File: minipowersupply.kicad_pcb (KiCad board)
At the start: 2 copper layers, 91 x 60.4 mm, 112 parts, among them J1 Conn_01x01_Female, J10 Conn_01x08_Male, J2 Conn_01x01_Female, J3 Conn_01x01_Female, J4 Conn_01x01_Female, J5 Conn_01x01_Female, J6 Conn_01x01_Female, J7 Conn_01x01_Female, J8 Conn_01x02_Female, J9 Conn_01x02_Female, Q1 BC817, U1 LM317_TO-220, U10 74HC4051, U11 74HC4051, U12 LM358, U13 LM358, U2 LM337_TO220, U3 LM7805_TO220, U4 ACS70331EOLCTR-2P5U3, U5 ACS70331EOLCTR-2P5U3, U6 ACS70331EOLCTR-2P5U3, U7 ACS70331EOLCTR-2P5U3, U8 ACS70331EOLCTR-2P5U3, U9 LM358

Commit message: new EMC-EMI layout with improved suppression
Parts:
- removed A1: Arduino_Nano_v3.x, Module:Arduino_Nano
- removed C1, C10, C11, C12, C13, C14, C15, C16, C17, C18, C19, C2, C22, C23, C24, C25, C27, C29, C3, C30, C31, C32, C33, C34, C35, C36, C38, C4, C5, C6, C7, C8, C9: 0.1uF, Capacitor_SMD:C_0603_1608Metric
- removed C20, C21: 150uF, Capacitor_SMD:C_Elec_8x6.2
- removed C26, C28: 1uF, Capacitor_SMD:C_0603_1608Metric
- removed D1, D2, D3, D4, D5, D6, D7, D8, D9: S1K-13-F, Diode_SMD:D_SMA
- removed F1: Fuse, Fuse:Fuseholder_Cylinder-5x20mm_Bulgin_FX0457_Horizontal_Closed
- removed J1, J2, J3, J4, J5, J6, J7: Conn_01x01_Female, Connector_PinHeader_2.54mm:PinHeader_1x01_P2.54mm_Vertical
- removed J10: Conn_01x08_Male, Connector_PinHeader_2.54mm:PinHeader_1x08_P2.54mm_Vertical
- removed J8, J9: Conn_01x02_Female, Connector_PinHeader_2.54mm:PinHeader_1x02_P2.54mm_Vertical
- removed Q1: BC817, Package_TO_SOT_SMD:SOT-23
- removed R1, R2: 240, Resistor_SMD:R_0603_1608Metric
- removed R10, R11, R12, R13, R14, R15, R16, R17, R18, R19, R20, R21, R22, R23, R24, R25, R26, R27, R28, R29, R30, R33, R34, R35, R36, R6, R7, R8, R9: 10k 0.01%, Resistor_SMD:R_0603_1608Metric
- removed R3: 4.420k, Resistor_SMD:R_0603_1608Metric
- removed R31, R32: 100k 0.01%, Resistor_SMD:R_0603_1608Metric
- removed R4: 698, Resistor_SMD:R_0603_1608Metric
- removed R5: 410, Resistor_SMD:R_0603_1608Metric
- removed TP1, TP2, TP3: TestPoint, TestPoint:TestPoint_THTPad_4.0x4.0mm_Drill2.0mm
- removed TR1: TRANSF3, minipowersupply:vtxtfr
- removed U1: LM317_TO-220, Package_TO_SOT_SMD:SOT-223-3_TabPin2
- removed U10, U11: 74HC4051, Package_SO:TSSOP-16_4.4x5mm_P0.65mm
- removed U12, U13, U9: LM358, Package_SO:TSSOP-8_4.4x3mm_P0.65mm
- removed U2: LM337_TO220, Package_TO_SOT_SMD:SOT-223-3_TabPin2
- removed U3: LM7805_TO220, Package_TO_SOT_SMD:SOT-223-3_TabPin2
- removed U4, U5, U6, U7, U8: ACS70331EOLCTR-2P5U3, ACS70331EOLCTR-2P5U3:SOIC127P600X175-8N
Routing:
- net GNDREF: track 289.1 -> 0.00 mm, vias 55 -> 0
- net VUnreg+: track 170.0 -> 0.00 mm, vias 6 -> 0
- net 3V3: track 164.9 -> 0.00 mm, vias 12 -> 0
- net VUnreg-: track 95.1 -> 0.00 mm, vias 8 -> 0
- net /Clock and TTL/Ck_Out: track 93.0 -> 0.00 mm, vias 1 -> 0
- net V5: track 90.4 -> 0.00 mm, vias 3 -> 0
- net /I V Sensor, Mux and output/A1: track 64.5 -> 0.00 mm, vias 4 -> 0
- net /I V Sensor, Mux and output/VU+: track 61.1 -> 0.00 mm, vias 2 -> 0
- net /I V Sensor, Mux and output/A3: track 60.8 -> 0.00 mm, vias 2 -> 0
- net /I V Sensor, Mux and output/A0: track 57.5 -> 0.00 mm, vias 2 -> 0
- net /I V Sensor, Mux and output/VA+: track 48.3 -> 0.00 mm, vias 1 -> 0
- net /I V Sensor, Mux and output/IU+: track 47.9 -> 0.00 mm, vias 2 -> 0
- net /I V Sensor, Mux and output/U- Unity Inverter/Ain: track 42.4 -> 0.00 mm, vias 2 -> 0
- net /I V Sensor, Mux and output/A2: track 42.2 -> 0.00 mm, vias 2 -> 0
- net /I V Sensor, Mux and output/A5: track 39.5 -> 0.00 mm
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- removed copper zone on B.Cu, net GNDREF
- removed copper zone on F.Cu, net GNDREF
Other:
- board outline removed
- board text removed: "5V"
- board text removed: "A+"
- board text removed: "A-"
- board text removed: "CK"
- board text removed: "Safety Cutouts"
- board text removed: "U+"
- board text removed: "U-"

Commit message: updates with foot print guard rings
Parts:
- added A1: Arduino_Nano_v3.x, Module:Arduino_Nano, F.Cu at (99.1, 125.7)
- added C1: 0.1uF, Capacitor_SMD:C_0603_1608Metric, B.Cu at (181.1, 66.5)
- added C10: 0.1uF, Capacitor_SMD:C_0603_1608Metric, F.Cu at (187.8, 96.4)
- added C11: 0.1uF, Capacitor_SMD:C_0603_1608Metric, F.Cu at (212.0, 73.6)
- added C12: 0.1uF, Capacitor_SMD:C_0603_1608Metric, F.Cu at (212.0, 77.0)
- added C13: 0.1uF, Capacitor_SMD:C_0603_1608Metric, F.Cu at (189.1, 106.5)
- added C14: 0.1uF, Capacitor_SMD:C_0603_1608Metric, F.Cu at (212.0, 83.7)
- added C15: 0.1uF, Capacitor_SMD:C_0603_1608Metric, F.Cu at (212.0, 86.8)
- added C16: 0.1uF, Capacitor_SMD:C_0603_1608Metric, F.Cu at (212.0, 89.3)
- added C17: 0.1uF, Capacitor_SMD:C_0603_1608Metric, F.Cu at (212.0, 92.5)
- added C18: 0.1uF, Capacitor_SMD:C_0603_1608Metric, F.Cu at (184.2, 112.4)
- added C19: 0.1uF, Capacitor_SMD:C_0603_1608Metric, F.Cu at (187.4, 118.5)
- added C2: 0.1uF, Capacitor_SMD:C_0603_1608Metric, B.Cu at (182.4, 66.5)
- added C20: 150uF, Capacitor_SMD:C_Elec_8x6.2, F.Cu at (140.0, 93.7)
- added C21: 150uF, Capacitor_SMD:C_Elec_8x6.2, F.Cu at (140.7, 64.6)
- added C22: 0.1uF, Capacitor_SMD:C_0603_1608Metric, F.Cu at (167.7, 75.7)
- added C23: 0.1uF, Capacitor_SMD:C_0603_1608Metric, F.Cu at (212.0, 110.8)
- added C24: 0.1uF, Capacitor_SMD:C_0603_1608Metric, F.Cu at (212.0, 113.9)
- added C25: 0.1uF, Capacitor_SMD:C_0603_1608Metric, F.Cu at (167.4, 60.3)
- added C26: 1uF, Capacitor_SMD:C_0603_1608Metric, F.Cu at (212.0, 120.1)
- added C27: 0.1uF, Capacitor_SMD:C_0603_1608Metric, F.Cu at (212.0, 122.7)
- added C28: 1uF, Capacitor_SMD:C_0603_1608Metric, F.Cu at (212.0, 125.6)
- added C29: 0.1uF, Capacitor_SMD:C_0603_1608Metric, F.Cu at (212.0, 128.6)
- added C3: 0.1uF, Capacitor_SMD:C_0603_1608Metric, F.Cu at (189.1, 66.6)
- added C30: 0.1uF, Capacitor_SMD:C_0603_1608Metric, F.Cu at (212.0, 131.8)
- added C31: 0.1uF, Capacitor_SMD:C_0603_1608Metric, F.Cu at (212.0, 134.9)
- added C32: 0.1uF, Capacitor_SMD:C_0603_1608Metric, B.Cu at (181.0, 55.9)
- added C33: 0.1uF, Capacitor_SMD:C_0603_1608Metric, B.Cu at (182.3, 55.9)
- added C34: 0.1uF, Capacitor_SMD:C_0603_1608Metric, F.Cu at (211.8, 143.5)
- added C35: 0.1uF, Capacitor_SMD:C_0603_1608Metric, B.Cu at (180.5, 105.8)
- added C36: 0.1uF, Capacitor_SMD:C_0603_1608Metric, B.Cu at (181.8, 105.8)
- added C38: 0.1uF, Capacitor_SMD:C_0603_1608Metric, F.Cu at (212.0, 148.7)
- added C4: 0.1uF, Capacitor_SMD:C_0603_1608Metric, B.Cu at (181.1, 75.9)
- added C5: 0.1uF, Capacitor_SMD:C_0603_1608Metric, B.Cu at (182.4, 75.9)
- added C6: 0.1uF, Capacitor_SMD:C_0603_1608Metric, F.Cu at (186.1, 55.2)
- added C7: 0.1uF, Capacitor_SMD:C_0603_1608Metric, B.Cu at (180.9, 95.7)
- added C8: 0.1uF, Capacitor_SMD:C_0603_1608Metric, B.Cu at (182.1, 95.7)
- added C9: 0.1uF, Capacitor_SMD:C_0603_1608Metric, F.Cu at (189.1, 76.7)
- added D1: S1K-13-F, Diode_SMD:D_SMA, B.Cu at (138.9, 71.4)
- added D2: S1K-13-F, Diode_SMD:D_SMA, B.Cu at (138.9, 86.4)
- added D3: S1K-13-F, Diode_SMD:D_SMA, F.Cu at (138.9, 71.4)
- added D4: S1K-13-F, Diode_SMD:D_SMA, F.Cu at (138.9, 86.4)
- added D5: S1K-13-F, Diode_SMD:D_SMA, F.Cu at (138.9, 79.5)
- added D6: S1K-13-F, Diode_SMD:D_SMA, B.Cu at (138.9, 79.5)
- added D7: S1K-13-F, Diode_SMD:D_SMA, F.Cu at (156.3, 83.7)
- added D8: S1K-13-F, Diode_SMD:D_SMA, F.Cu at (160.0, 83.7)
- added F1: Fuse, Fuse:Fuseholder_Cylinder-5x20mm_Bulgin_FX0457_Horizontal_Closed, F.Cu at (94.7, 90.4)
- added FB1: FerriteBead_Small, Inductor_SMD:L_0603_1608Metric, F.Cu at (220.5, 43.6)
- added FB10: FerriteBead_Small, Inductor_SMD:L_0603_1608Metric, F.Cu at (222.0, 73.5)
- added FB11: FerriteBead_Small, Inductor_SMD:L_0603_1608Metric, F.Cu at (221.7, 77.7)
- added FB12: FerriteBead_Small, Inductor_SMD:L_0603_1608Metric, F.Cu at (220.7, 81.4)
- added FB13: FerriteBead_Small, Inductor_SMD:L_0603_1608Metric, F.Cu at (169.4, 78.8)
- added FB14: FerriteBead_Small, Inductor_SMD:L_0603_1608Metric, F.Cu at (169.4, 85.0)
- added FB15: FerriteBead_Small, Inductor_SMD:L_0603_1608Metric, F.Cu at (221.2, 88.9)
- added FB16: FerriteBead_Small, Inductor_SMD:L_0603_1608Metric, F.Cu at (221.6, 96.8)
- added FB17: FerriteBead_Small, Inductor_SMD:L_0603_1608Metric, F.Cu at (221.5, 92.8)
- added FB2: FerriteBead_Small, Inductor_SMD:L_0603_1608Metric, F.Cu at (220.7, 47.5)
- added FB3: FerriteBead_Small, Inductor_SMD:L_0603_1608Metric, F.Cu at (151.8, 76.9)
- added FB4: FerriteBead_Small, Inductor_SMD:L_0603_1608Metric, F.Cu at (151.9, 62.4)
- added FB5: FerriteBead_Small, Inductor_SMD:L_0603_1608Metric, F.Cu at (152.6, 94.2)
- added FB6: FerriteBead_Small, Inductor_SMD:L_0603_1608Metric, F.Cu at (223.5, 50.8)
- added FB7: FerriteBead_Small, Inductor_SMD:L_0603_1608Metric, F.Cu at (221.1, 62.5)
- added FB8: FerriteBead_Small, Inductor_SMD:L_0603_1608Metric, F.Cu at (224.2, 65.7)
- added FB9: FerriteBead_Small, Inductor_SMD:L_0603_1608Metric, F.Cu at (222.0, 69.3)
- added J1: Conn_01x01_Female, Connector_PinHeader_2.54mm:PinHeader_1x01_P2.54mm_Vertical, F.Cu at (189.5, 54.1)
- added J10: Conn_01x08_Male, Connector_PinHeader_2.54mm:PinHeader_1x08_P2.54mm_Vertical, F.Cu at (89.3, 127.4)
- added J2: Conn_01x01_Female, Connector_PinHeader_2.54mm:PinHeader_1x01_P2.54mm_Vertical, F.Cu at (189.4, 64.0)
- added J3: Conn_01x01_Female, Connector_PinHeader_2.54mm:PinHeader_1x01_P2.54mm_Vertical, F.Cu at (189.5, 74.1)
- added J4: Conn_01x01_Female, Connector_PinHeader_2.54mm:PinHeader_1x01_P2.54mm_Vertical, F.Cu at (189.5, 82.4)
- added J5: Conn_01x01_Female, Connector_PinHeader_2.54mm:PinHeader_1x01_P2.54mm_Vertical, F.Cu at (189.5, 86.6)
- added J6: Conn_01x01_Female, Connector_PinHeader_2.54mm:PinHeader_1x01_P2.54mm_Vertical, F.Cu at (189.5, 93.8)
- added J7: Conn_01x01_Female, Connector_PinHeader_2.54mm:PinHeader_1x01_P2.54mm_Vertical, F.Cu at (189.5, 103.9)
- added J8: Conn_01x02_Female, Connector_PinHeader_2.54mm:PinHeader_1x02_P2.54mm_Vertical, F.Cu at (172.6, 67.0)
- added J9: Conn_01x02_Female, Connector_PinHeader_2.54mm:PinHeader_1x02_P2.54mm_Vertical, F.Cu at (169.7, 96.3)
- added Q1: BC817, Package_TO_SOT_SMD:SOT-23, F.Cu at (165.9, 84.1)
- added R1: 240, Resistor_SMD:R_0603_1608Metric, F.Cu at (169.8, 64.3)
- added R10: 10k 0.01%, Resistor_SMD:R_0603_1608Metric, B.Cu at (186.8, 65.1)
- added R11: 10k 0.01%, Resistor_SMD:R_0603_1608Metric, F.Cu at (186.0, 65.9)
- added R12: 10k 0.01%, Resistor_SMD:R_0603_1608Metric, F.Cu at (186.8, 73.3)
- added R13: 10k 0.01%, Resistor_SMD:R_0603_1608Metric, B.Cu at (186.8, 75.0)
- added R14: 10k 0.01%, Resistor_SMD:R_0603_1608Metric, F.Cu at (186.0, 75.8)
- added R15: 10k 0.01%, Resistor_SMD:R_0603_1608Metric, F.Cu at (186.9, 92.4)
- added R16: 10k 0.01%, Resistor_SMD:R_0603_1608Metric, B.Cu at (186.9, 94.0)
- added R17: 10k 0.01%, Resistor_SMD:R_0603_1608Metric, F.Cu at (186.1, 94.9)
- added R18: 10k 0.01%, Resistor_SMD:R_0603_1608Metric, F.Cu at (187.0, 102.5)
- added R19: 10k 0.01%, Resistor_SMD:R_0603_1608Metric, B.Cu at (187.0, 104.2)
- added R2: 240, Resistor_SMD:R_0603_1608Metric, F.Cu at (166.4, 92.7)
- added R20: 10k 0.01%, Resistor_SMD:R_0603_1608Metric, F.Cu at (186.2, 105.0)
- added R21: 10k 0.01%, Resistor_SMD:R_0603_1608Metric, F.Cu at (204.6, 99.4)
- added R22: 10k 0.01%, Resistor_SMD:R_0603_1608Metric, F.Cu at (204.6, 102.5)
- added R23: 10k 0.01%, Resistor_SMD:R_0603_1608Metric, F.Cu at (185.7, 112.4)
- added R24: 10k 0.01%, Resistor_SMD:R_0603_1608Metric, F.Cu at (187.3, 112.4)
- added R25: 10k 0.01%, Resistor_SMD:R_0603_1608Metric, F.Cu at (204.6, 111.7)
- added R26: 10k 0.01%, Resistor_SMD:R_0603_1608Metric, F.Cu at (204.6, 114.6)
- added R27: 10k 0.01%, Resistor_SMD:R_0603_1608Metric, F.Cu at (204.6, 117.8)
- added R28: 10k 0.01%, Resistor_SMD:R_0603_1608Metric, F.Cu at (204.6, 120.7)
- added R29: 10k 0.01%, Resistor_SMD:R_0603_1608Metric, F.Cu at (204.6, 123.6)
- added R3: 4.420k, Resistor_SMD:R_0603_1608Metric, F.Cu at (152.4, 85.7)
- added R30: 10k 0.01%, Resistor_SMD:R_0603_1608Metric, F.Cu at (204.6, 126.6)
- added R31: 100k 0.01%, Resistor_SMD:R_0603_1608Metric, F.Cu at (204.6, 129.7)
- added R32: 100k 0.01%, Resistor_SMD:R_0603_1608Metric, F.Cu at (204.6, 132.9)
- added R33: 10k 0.01%, Resistor_SMD:R_0603_1608Metric, F.Cu at (204.6, 135.0)
- added R34: 10k 0.01%, Resistor_SMD:R_0603_1608Metric, F.Cu at (204.7, 137.9)
- added R35: 10k 0.01%, Resistor_SMD:R_0603_1608Metric, F.Cu at (204.7, 140.7)
- added R4: 698, Resistor_SMD:R_0603_1608Metric, F.Cu at (162.9, 84.0)
- added R5: 410, Resistor_SMD:R_0603_1608Metric, F.Cu at (169.4, 81.9)
- added R6: 10k 0.01%, Resistor_SMD:R_0603_1608Metric, F.Cu at (186.8, 52.8)
- added R7: 10k 0.01%, Resistor_SMD:R_0603_1608Metric, B.Cu at (186.8, 54.4)
- added R8: 10k 0.01%, Resistor_SMD:R_0603_1608Metric, F.Cu at (187.7, 56.8)
- added R9: 10k 0.01%, Resistor_SMD:R_0603_1608Metric, F.Cu at (186.8, 63.4)
- added TP1: TestPoint, TestPoint:TestPoint_THTPad_4.0x4.0mm_Drill2.0mm, F.Cu at (79.8, 82.0)
- added TP2: TestPoint, TestPoint:TestPoint_THTPad_4.0x4.0mm_Drill2.0mm, F.Cu at (79.9, 76.1)
- added TP3: TestPoint, TestPoint:TestPoint_THTPad_4.0x4.0mm_Drill2.0mm, F.Cu at (79.8, 88.1)
- added TR1: TRANSF3, minipowersupply:vtxtfr, F.Cu at (119.8, 79.2)
- added U1: LM317_TO-220, Package_TO_SOT_SMD:SOT-223-3_TabPin2, F.Cu at (162.3, 64.6)
- added U10: 74HC4051, Package_SO:TSSOP-16_4.4x5mm_P0.65mm, F.Cu at (170.8, 120.6)
- added U11: 74HC4051, Package_SO:TSSOP-16_4.4x5mm_P0.65mm, F.Cu at (181.9, 121.1)
- added U12: LM358, Package_SO:TSSOP-8_4.4x3mm_P0.65mm, F.Cu at (164.7, 114.8)
- added U13: LM358, Package_SO:TSSOP-8_4.4x3mm_P0.65mm, F.Cu at (162.4, 124.7)
- added U2: LM337_TO220, Package_TO_SOT_SMD:SOT-223-3_TabPin2, F.Cu at (160.4, 94.1)
- added U3: LM7805_TO220, Package_TO_SOT_SMD:SOT-223-3_TabPin2, F.Cu at (162.4, 74.6)
- added U4: ACS70331EOLCTR-2P5U3, ACS70331EOLCTR-2P5U3:SOIC127P600X175-8N, F.Cu at (180.4, 54.4)
- added U5: ACS70331EOLCTR-2P5U3, ACS70331EOLCTR-2P5U3:SOIC127P600X175-8N, F.Cu at (180.4, 64.9)
- added U6: ACS70331EOLCTR-2P5U3, ACS70331EOLCTR-2P5U3:SOIC127P600X175-8N, F.Cu at (180.5, 74.9)
- added U7: ACS70331EOLCTR-2P5U3, ACS70331EOLCTR-2P5U3:SOIC127P600X175-8N, F.Cu at (180.2, 94.1)
- added U8: ACS70331EOLCTR-2P5U3, ACS70331EOLCTR-2P5U3:SOIC127P600X175-8N, F.Cu at (179.9, 104.2)
- added U9: LM358, Package_SO:TSSOP-8_4.4x3mm_P0.65mm, F.Cu at (189.0, 116.0)
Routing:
- net (no net): track 0.00 -> 301.8 mm
- net GNDREF: track 0.00 -> 143.8 mm, vias 0 -> 12
- net VUnreg+: track 0.00 -> 84.3 mm
- net VUnreg-: track 0.00 -> 75.0 mm, vias 0 -> 1
- net /I V Sensor, Mux and output/IU+: track 0.00 -> 74.6 mm, vias 0 -> 2
- net /I V Sensor, Mux and output/VU+: track 0.00 -> 71.4 mm, vias 0 -> 2
- net /I V Sensor, Mux and output/IA+: track 0.00 -> 57.6 mm, vias 0 -> 2
- net 3V3: track 0.00 -> 57.4 mm, vias 0 -> 5
- net /I V Sensor, Mux and output/VA+: track 0.00 -> 55.5 mm, vias 0 -> 2
- net /I V Sensor, Mux and output/I5: track 0.00 -> 48.2 mm, vias 0 -> 2
- net /I V Sensor, Mux and output/V5+: track 0.00 -> 45.9 mm, vias 0 -> 2
- net /I V Sensor, Mux and output/IA-: track 0.00 -> 28.2 mm, vias 0 -> 2
- net /Clock and TTL/Ck_Out: track 0.00 -> 25.0 mm
- net /Clock and TTL/V5Out: track 0.00 -> 21.5 mm
- net /DualAdj/Vreg+: track 0.00 -> 21.2 mm
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- added copper zone on B.Cu, net GNDREF
- added copper zone on F.Cu, net GNDREF
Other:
- board outline added: 127.2 x 85.6 mm

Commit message: New board layout
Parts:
- moved FB10 126.5 mm to (99.2, 103.8), turned to -90 degrees
- moved FB8 91.7 mm to (145.0, 111.9), turned to 180 degrees
- moved FB9 91.2 mm to (139.0, 107.1), turned to 180 degrees
- moved FB1 87.9 mm to (155.4, 102.6), turned to -90 degrees
- moved FB2 83.0 mm to (158.6, 102.5), turned to 90 degrees
- moved FB6 82.1 mm to (168.4, 111.7), turned to 135 degrees
- moved FB17 67.8 mm to (158.1, 116.8), turned to -45 degrees
- moved FB15 65.2 mm to (160.2, 112.2), turned to 135 degrees
- moved FB16 65.2 mm to (164.7, 128.5), turned to 135 degrees
- moved C27 51.6 mm to (166.3, 98.7)
- moved R26 45.7 mm to (159.3, 120.1), turned to 135 degrees
- moved R25 44.9 mm to (160.4, 119.0), turned to -45 degrees
- moved C11 22.5 mm to (212.3, 51.1)
- moved C20 7.59 mm to (147.6, 93.7)
- moved C21 7.59 mm to (148.3, 64.6)
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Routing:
- net GNDREF: track 143.8 -> 298.2 mm, vias 12 -> 24
- net VUnreg+: track 84.3 -> 194.1 mm
- net (no net): track 301.8 -> 209.0 mm
- net Net-(A1-Pad27): track 0.00 -> 86.0 mm
- net /I V Sensor, Mux and output/A0: track 0.00 -> 73.4 mm
- net /I V Sensor, Mux and output/A3: track 0.00 -> 72.9 mm
- net /I V Sensor, Mux and output/A1: track 0.00 -> 70.8 mm
- net /I V Sensor, Mux and output/A4: track 0.00 -> 70.3 mm
- net /I V Sensor, Mux and output/A2: track 0.00 -> 67.9 mm
- net /I V Sensor, Mux and output/A5: track 0.00 -> 66.5 mm
- net Net-(A1-Pad17): track 0.00 -> 52.3 mm, vias 0 -> 3
- net VUnreg-: track 75.0 -> 122.0 mm, vias 1 -> 2
- net /Measure/SDA: track 0.00 -> 35.9 mm
- net Net-(A1-Pad9): track 0.00 -> 32.8 mm, vias 0 -> 2
- net Net-(A1-Pad8): track 0.00 -> 30.6 mm, vias 0 -> 2
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- added copper zone on F.Cu, net /DualAdj/Vreg+
- added copper zone on F.Cu, net Net-(C27-Pad1)

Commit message: working on MUX and pre-amp layout
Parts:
- added C37: 0.1uF, Capacitor_SMD:C_0603_1608Metric, F.Cu at (155.7, 122.9)
- moved FB7 82.1 mm to (165.8, 123.1), turned to 135 degrees
- moved C15 78.2 mm to (145.1, 127.4)
- moved C14 76.1 mm to (147.6, 124.2)
- moved FB11 72.5 mm to (153.7, 102.6), turned to -90 degrees
- moved C16 72.4 mm to (147.6, 122.5)
- moved C26 71.6 mm to (167.6, 63.9), turned to 90 degrees
- moved C34 68.0 mm to (147.7, 120.6)
- moved FB12 63.6 mm to (160.7, 102.6), turned to 90 degrees
- moved C11 63.4 mm to (192.7, 111.4)
- moved C31 60.5 mm to (158.0, 107.6), turned to -45 degrees
- moved C23 58.2 mm to (167.7, 73.1), turned to -90 degrees
- moved R35 58.1 mm to (148.3, 127.2), turned to 90 degrees
- moved F1 56.3 mm to (138.8, 55.4), turned to 180 degrees
- moved C24 54.4 mm to (168.4, 81.4), turned to 180 degrees
- moved C28 50.6 mm to (173.8, 92.4), turned to 90 degrees
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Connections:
- A1 pad 5: unconnected-(A1-Pad5) -> Net-(A1-Pad5)
- A1 pad 6: unconnected-(A1-Pad6) -> Net-(A1-Pad6)
- A1 pad 8: Net-(A1-Pad8) -> unconnected-(A1-Pad8)
- A1 pad 9: Net-(A1-Pad9) -> unconnected-(A1-Pad9)
- FB2 pad 1: Net-(C12-Pad1) -> VUnreg-
- FB2 pad 2: VUnreg- -> Net-(C12-Pad1)
- J10 pad 1: Net-(A1-Pad7) -> Net-(A1-Pad5)
- J10 pad 2: Net-(A1-Pad8) -> Net-(A1-Pad6)
- J10 pad 3: Net-(A1-Pad9) -> Net-(A1-Pad7)
- U12 pad 5: Net-(FB6-Pad2) -> Net-(R29-Pad1)
- U12 pad 6: Net-(C31-Pad2) -> Net-(R27-Pad2)
- U12 pad 7: Net-(C31-Pad2) -> Net-(R32-Pad1)
- U13 pad 5: Net-(R29-Pad1) -> Net-(FB6-Pad2)
- U13 pad 6: Net-(R27-Pad2) -> Net-(C31-Pad2)
- U13 pad 7: Net-(R32-Pad1) -> Net-(C31-Pad2)
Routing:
- net Net-(A1-Pad21): track 0.00 -> 61.5 mm, vias 0 -> 1
- net VUnreg-: track 122.0 -> 66.4 mm, vias 2 -> 1
- net VUnreg+: track 194.1 -> 144.3 mm
- net Net-(F1-Pad1): track 0.00 -> 44.4 mm
- net Net-(A1-Pad9): track 32.8 -> 0.00 mm, vias 2 -> 0
- net unconnected-(A1-Pad8): track 0.00 -> 30.6 mm, vias 0 -> 2
- net Net-(A1-Pad8): track 30.6 -> 0.00 mm, vias 2 -> 0
- net Net-(F1-Pad2): track 0.00 -> 28.8 mm
- net Net-(A1-Pad5): track 0.00 -> 28.3 mm, vias 0 -> 2
- net (no net): track 209.0 -> 184.3 mm
- net Net-(TP2-Pad1): track 0.00 -> 14.5 mm
- net GNDREF: track 298.2 -> 307.3 mm, vias 24 -> 29
- net /Clock and TTL/HalfSineIn: track 15.6 -> 8.01 mm
- net Net-(C31-Pad2): track 7.13 -> 0.00 mm
- net Net-(C27-Pad1): track 16.0 -> 10.5 mm
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
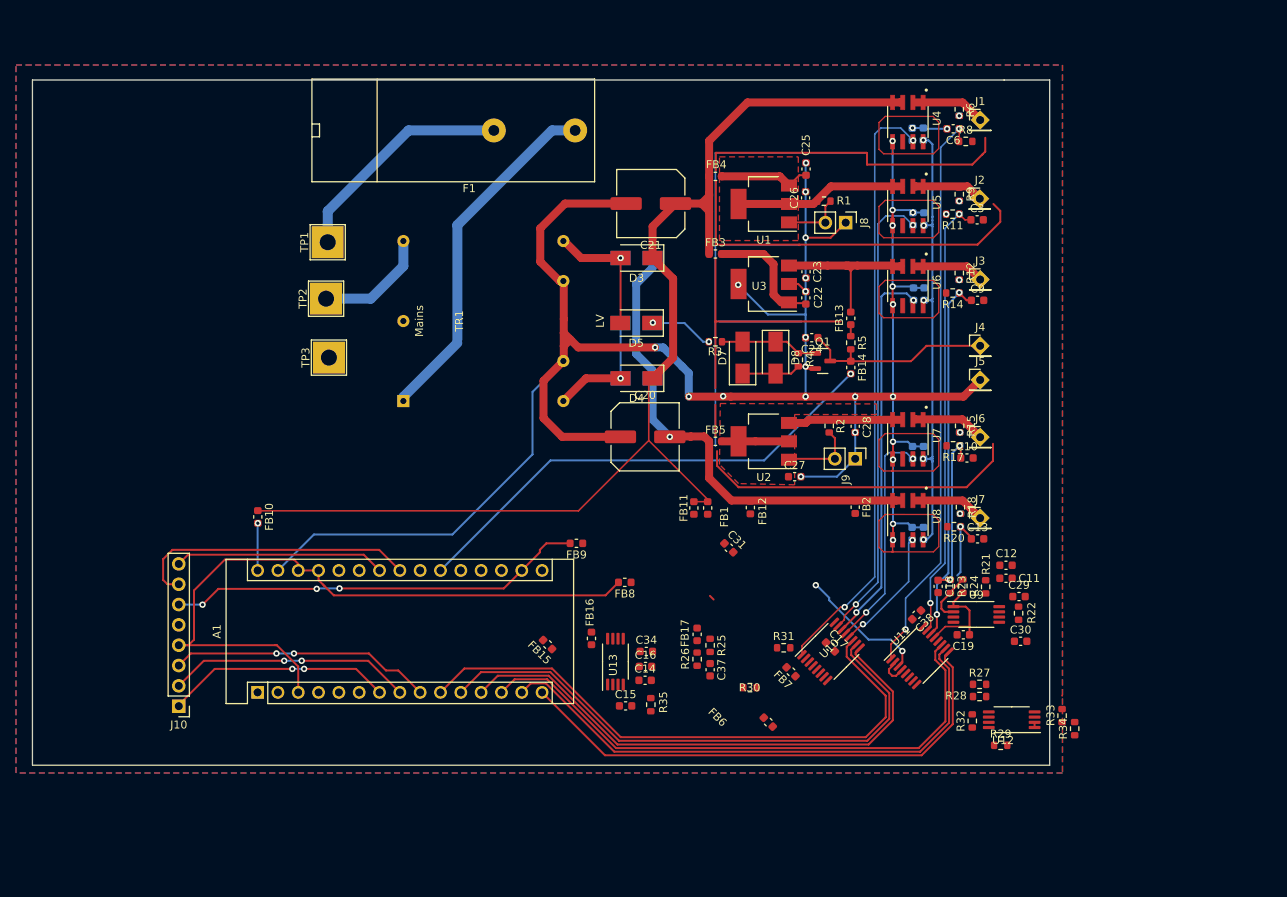
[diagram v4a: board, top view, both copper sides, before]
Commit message: mux and opamp layouts completed and new ext conn to display
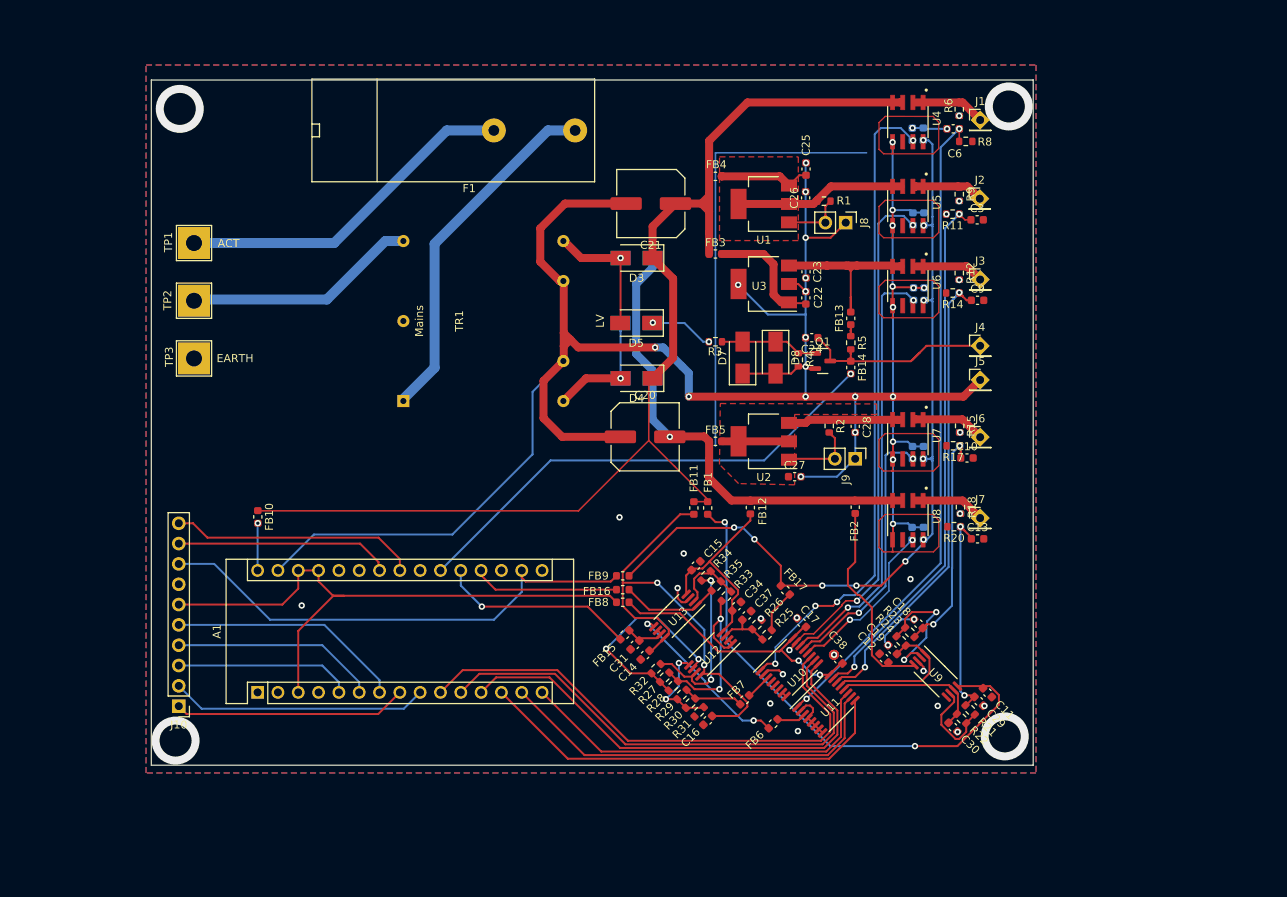
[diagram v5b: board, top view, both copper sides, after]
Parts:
- J10: footprint Connector_PinHeader_2.54mm:PinHeader_1x08_P2.54mm_Vertical -> Connector_PinHeader_2.54mm:PinHeader_1x10_P2.54mm_Vertical
- moved R34 49.9 mm to (155.2, 111.1), turned to 45 degrees
- moved R33 44.5 mm to (157.7, 113.7), turned to 45 degrees
- moved R29 40.4 mm to (152.2, 126.0), turned to 45 degrees
- moved R32 40.1 mm to (148.9, 122.7), turned to -135 degrees
- moved R27 39.4 mm to (150.0, 123.8), turned to -135 degrees
- moved U12 38.5 mm to (155.8, 120.9), turned to -135 degrees
- moved R28 38.3 mm to (151.1, 124.9), turned to -135 degrees
- moved C15 19.6 mm to (153.9, 109.9), turned to 45 degrees
- moved C12 19.2 mm to (177.4, 121.4), turned to 135 degrees
- moved R35 16.9 mm to (156.5, 112.4), turned to -135 degrees
- moved C31 16.9 mm to (146.3, 119.8), turned to 45 degrees
- moved TP3 16.9 mm to (91.2, 83.9)
- moved TP1 16.7 mm to (91.2, 69.5)
- moved TP2 16.5 mm to (91.2, 76.7)
- moved R21 15.5 mm to (188.2, 127.9), turned to -45 degrees
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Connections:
- A1 pad 8: unconnected-(A1-Pad8) -> Net-(A1-Pad8)
- A1 pad 9: unconnected-(A1-Pad9) -> Net-(A1-Pad9)
- J10 pad 1: Net-(A1-Pad5) -> Net-(A1-Pad8)
- J10 pad 2: Net-(A1-Pad6) -> Net-(A1-Pad9)
- J10 pad 3: Net-(A1-Pad7) -> Net-(A1-Pad5)
- J10 pad 4: Net-(A1-Pad27) -> Net-(A1-Pad6)
- J10 pad 5: GNDREF -> Net-(A1-Pad7)
- J10 pad 6: Net-(A1-Pad17) -> Net-(A1-Pad27)
- J10 pad 7: /Measure/SDA -> GNDREF
- J10 pad 8: /Measure/SCL -> Net-(A1-Pad17)
- U11 pad 11: /I V Sensor, Mux and output/A3 -> /I V Sensor, Mux and output/A5
- U11 pad 9: /I V Sensor, Mux and output/A5 -> /I V Sensor, Mux and output/A3
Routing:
- net (no net): track 184.3 -> 0.00 mm
- net Net-(C11-Pad1): track 0.00 -> 66.1 mm, vias 0 -> 2
- net Net-(C14-Pad1): track 0.00 -> 58.5 mm, vias 0 -> 2
- net 3V3: track 56.3 -> 104.1 mm, vias 5 -> 10
- net V5: track 0.00 -> 35.5 mm, vias 0 -> 2
- net Net-(A1-Pad9): track 0.00 -> 32.2 mm
- net unconnected-(A1-Pad8): track 30.6 -> 0.00 mm, vias 2 -> 0
- net Net-(A1-Pad8): track 0.00 -> 29.2 mm
- net Net-(R27-Pad2): track 0.00 -> 26.8 mm, vias 0 -> 2
- net Net-(A1-Pad6): track 0.00 -> 25.7 mm
- net Net-(C12-Pad1): track 0.00 -> 25.4 mm
- net Net-(C15-Pad1): track 0.00 -> 25.3 mm
- net Net-(A1-Pad20): track 0.00 -> 24.6 mm, vias 0 -> 1
- net Net-(R27-Pad1): track 1.30 -> 24.7 mm, vias 0 -> 2
- net Net-(R32-Pad1): track 0.00 -> 22.2 mm, vias 0 -> 2
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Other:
- board size 127.2 x 85.6 mm -> 110.2 x 85.7 mm
- board text added: "ACT"
- board text added: "EARTH"
